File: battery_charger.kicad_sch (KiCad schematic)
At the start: 0 parts

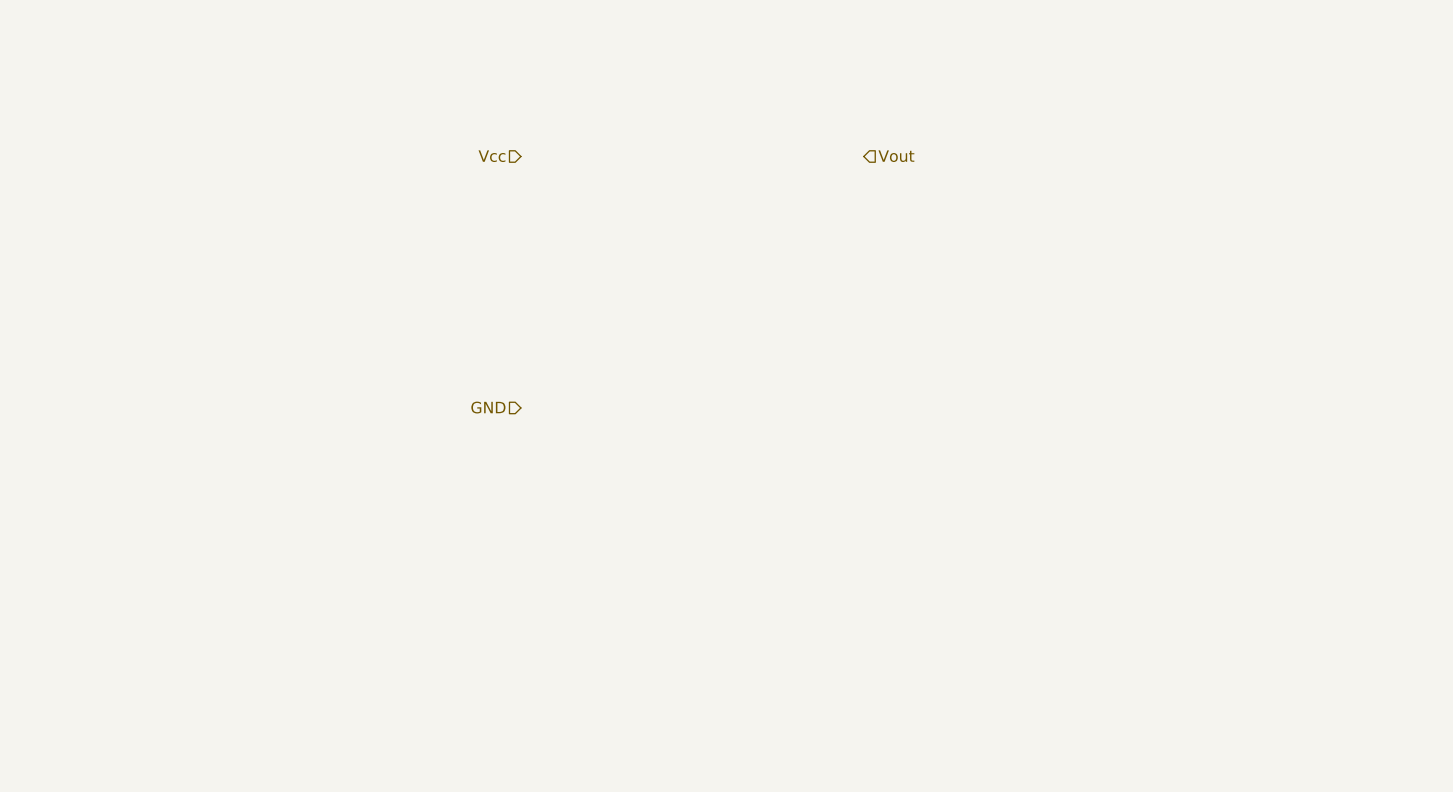
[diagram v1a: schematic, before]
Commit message: added symbols for battery charger module
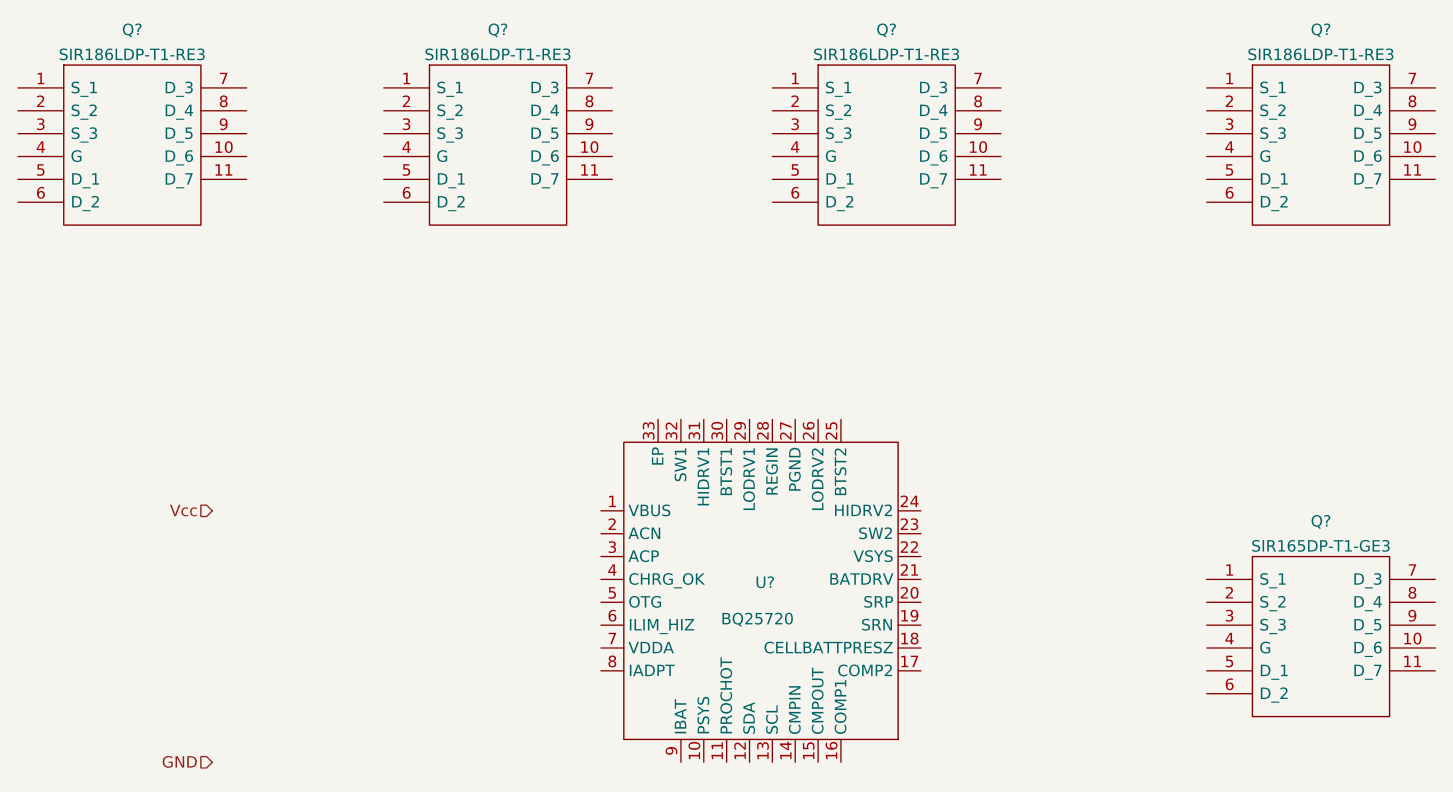
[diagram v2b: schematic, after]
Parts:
- added Q? (x4): SIR186LDP-T1-RE3, SamacSys_Parts:SI7141DPT1GE3, symbol sir186ldp-t1-re3:SIR186LDP-T1-RE3
- added Q?: SIR165DP-T1-GE3, SamacSys_Parts:SI7141DPT1GE3, symbol sir165dp-t1-ge3:SIR165DP-T1-GE3
- added U?: BQ25720, userdef:QFN-32_EP_4x4_Pitch0.4mm, symbol bq25720:BQ25720

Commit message: updated for winter 2022
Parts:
- gave numbers to parts that had none: 6
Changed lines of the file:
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@@
   (symbol (lib_id "sir186ldp-t1-re3:SIR186LDP-T1-RE3") (at 66.04 57.15 0) (unit 1)
     (in_bom yes) (on_board yes) (fields_autoplaced)
-    (property "Reference" "Q?" (id 0) (at 78.74 50.6942 0))
+    (property "Reference" "Q1" (id 0) (at 78.74 50.6942 0))
     (property "Value" "SIR186LDP-T1-RE3" (id 1) (at 78.74 53.4693 0))
     (property "Footprint" "SamacSys_Parts:SI7141DPT1GE3" (id 2) (at 87.63 54.61 0)
@@
   (symbol (lib_id "sir186ldp-t1-re3:SIR186LDP-T1-RE3") (at 106.68 57.15 0) (unit 1)
     (in_bom yes) (on_board yes) (fields_autoplaced)
-    (property "Reference" "Q?" (id 0) (at 119.38 50.6942 0))
+    (property "Reference" "Q2" (id 0) (at 119.38 50.6942 0))
     (property "Value" "SIR186LDP-T1-RE3" (id 1) (at 119.38 53.4693 0))
     (property "Footprint" "SamacSys_Parts:SI7141DPT1GE3" (id 2) (at 128.27 54.61 0)
@@
   (symbol (lib_id "sir186ldp-t1-re3:SIR186LDP-T1-RE3") (at 149.86 57.15 0) (unit 1)
     (in_bom yes) (on_board yes) (fields_autoplaced)
-    (property "Reference" "Q?" (id 0) (at 162.56 50.6942 0))
+    (property "Reference" "Q3" (id 0) (at 162.56 50.6942 0))
     (property "Value" "SIR186LDP-T1-RE3" (id 1) (at 162.56 53.4693 0))
     (property "Footprint" "SamacSys_Parts:SI7141DPT1GE3" (id 2) (at 171.45 54.61 0)
@@
   (symbol (lib_id "sir186ldp-t1-re3:SIR186LDP-T1-RE3") (at 198.12 57.15 0) (unit 1)
     (in_bom yes) (on_board yes) (fields_autoplaced)
-    (property "Reference" "Q?" (id 0) (at 210.82 50.6942 0))
+    (property "Reference" "Q4" (id 0) (at 210.82 50.6942 0))
     (property "Value" "SIR186LDP-T1-RE3" (id 1) (at 210.82 53.4693 0))
     (property "Footprint" "SamacSys_Parts:SI7141DPT1GE3" (id 2) (at 219.71 54.61 0)
@@
   (symbol (lib_id "sir165dp-t1-ge3:SIR165DP-T1-GE3") (at 198.12 111.76 0) (unit 1)
     (in_bom yes) (on_board yes) (fields_autoplaced)
-    (property "Reference" "Q?" (id 0) (at 210.82 105.3042 0))
+    (property "Reference" "Q5" (id 0) (at 210.82 105.3042 0))
     (property "Value" "SIR165DP-T1-GE3" (id 1) (at 210.82 108.0793 0))
     (property "Footprint" "SamacSys_Parts:SI7141DPT1GE3" (id 2) (at 219.71 109.22 0)
@@
   (symbol (lib_id "bq25720:BQ25720") (at 148.59 113.03 0) (unit 1)
     (in_bom yes) (on_board yes)
-    (property "Reference" "U?" (id 0) (at 147.9551 112.1215 0)
+    (property "Reference" "U5" (id 0) (at 147.9551 112.1215 0)
       (effects (font (size 1.27 1.27)) (justify left))
     )
